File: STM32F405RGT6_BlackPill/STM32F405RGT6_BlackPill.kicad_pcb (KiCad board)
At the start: 4 copper layers, 60 x 40 mm, 57 parts, among them J100 Conn_01x04, J101 Conn_02x15_Odd_Even, J102 Conn_02x10_Odd_Even, J200 USB_C_Receptacle_USB2.0_16P, U100 STM32F405RGTx, U200 USBLC6-2SC6, U201 ACM2012-900-2P-T001, U300 TLV62569DBV, Y1 32768Hz, Y100 25Mhz

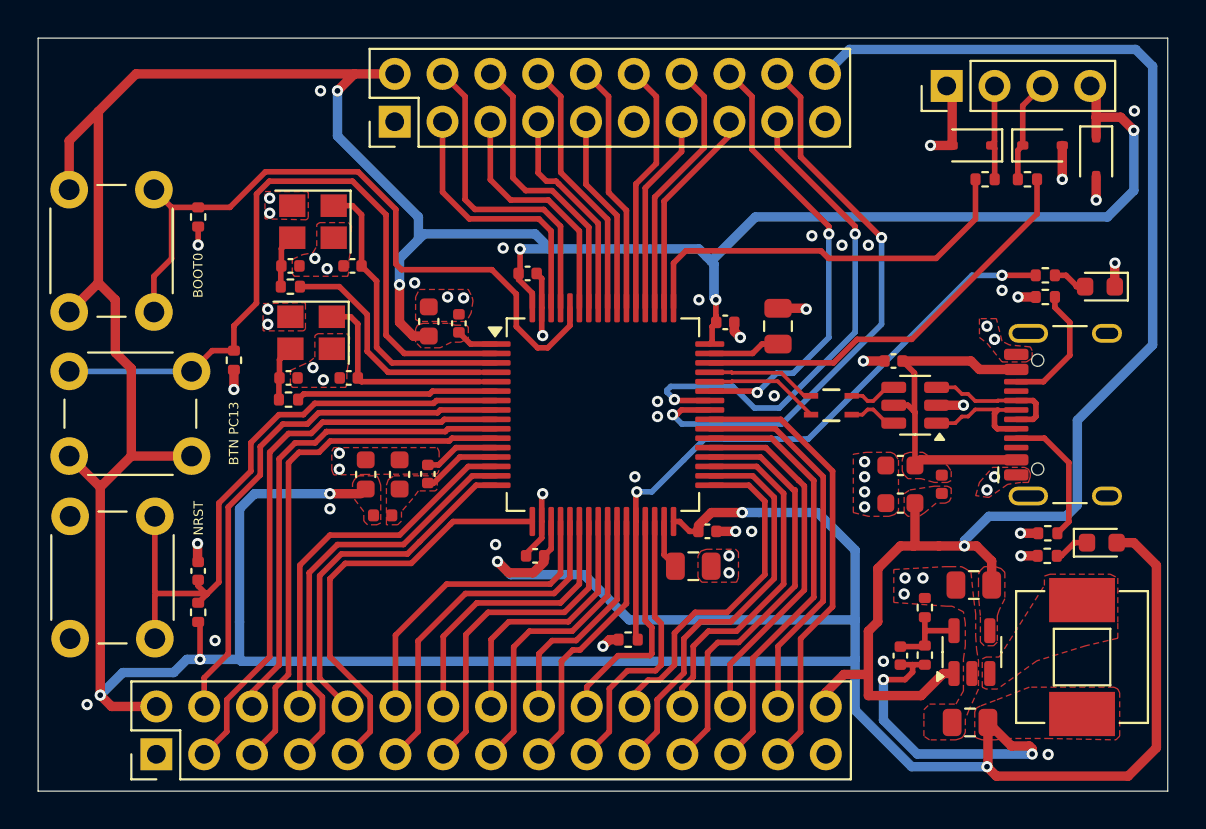
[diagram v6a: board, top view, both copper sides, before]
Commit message: VBUS | GND connector, manufacture files
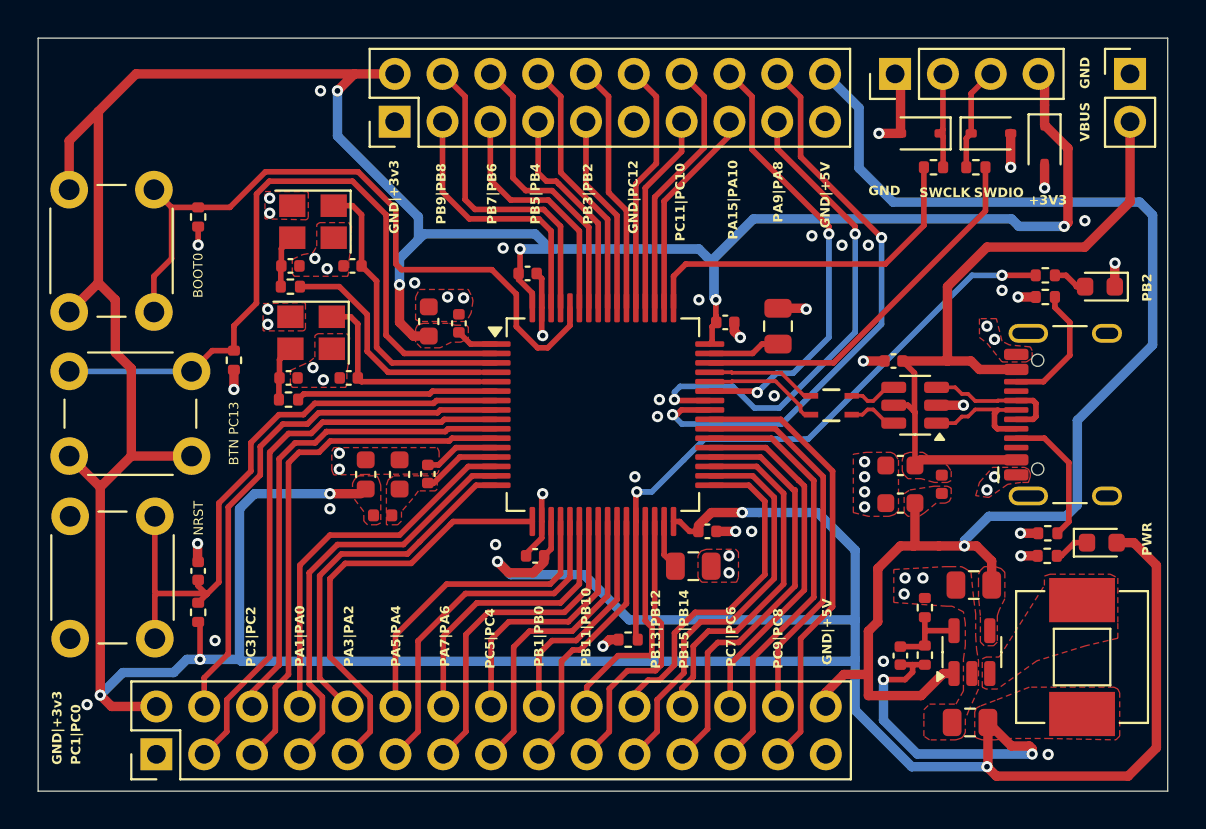
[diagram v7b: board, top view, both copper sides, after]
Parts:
- added J103: Conn_01x02, Connector_PinHeader_2.54mm:PinHeader_1x02_P2.54mm_Vertical, F.Cu at (136.1, 36.9)
- moved D100 2.81 mm to (131.6, 40.7)
- moved D102 2.81 mm to (125.0, 40.1)
- moved R105 2.81 mm to (127.9, 41.9)
- moved R106 2.81 mm to (125.7, 41.9)
- moved J100 2.81 mm to (123.6, 36.9)
- moved D101 2.81 mm to (128.7, 40.1)
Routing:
- net VBUS: track 18.8 -> 38.6 mm
- net +5V: track 76.2 -> 72.4 mm
- net +3.3V: track 296.6 -> 293.0 mm
- net SWCLK: track 21.8 -> 19.2 mm
- net SWDIO: track 22.5 -> 20.3 mm
- net PA9: track 27.7 -> 27.1 mm
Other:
- board text added: "+3V3"
- board text added: "GND"
- board text added: "GND|+3v3"
- board text added: "GND|+5V"
- board text added: "GND|PC12"
- board text added: "PA15|PA10"
- board text added: "PA1|PA0"
- board text added: "PA3|PA2"
- board text added: "PA5|PA4"
- board text added: "PA7|PA6"
- board text added: "PA9|PA8"
- board text added: "PB11|PB10"
- board text added: "PB13|PB12"
- board text added: "PB15|PB14"
- board text added: "PB1|PB0"
- board text added: "PB2"
- board text added: "PB3|PB2"
- board text added: "PB5|PB4"
- board text added: "PB7|PB6"
- board text added: "PB9|PB8"
- board text added: "PC11|PC10"
- board text added: "PC1|PC0"
- board text added: "PC3|PC2"
- board text added: "PC5|PC4"
- board text added: "PC7|PC6"
- board text added: "PC9|PC8"
- board text added: "PWR"
- board text added: "SWCLK"
- board text added: "SWDIO"
- board text added: "VBUS"

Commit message: Production files JLCPCB
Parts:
- renumbered Y1 to Y101
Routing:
- net /USB/USB_CONN_D-: track 6.69 -> 7.22 mm
